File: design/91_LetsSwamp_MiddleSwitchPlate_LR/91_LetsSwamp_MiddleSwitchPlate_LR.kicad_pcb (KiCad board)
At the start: 2 copper layers, 122.6 x 93.3 mm, 0 parts

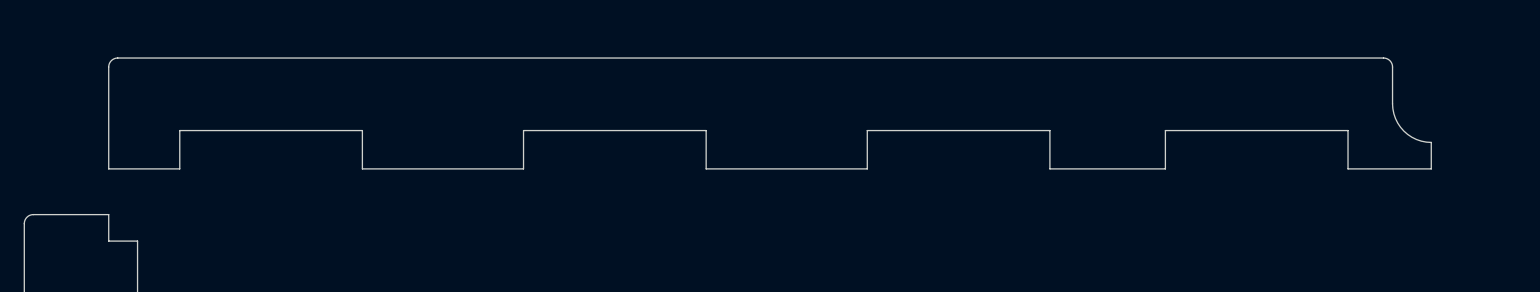
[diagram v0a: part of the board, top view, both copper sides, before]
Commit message: Modify middle plates
avoid to pin sockets and some diodes
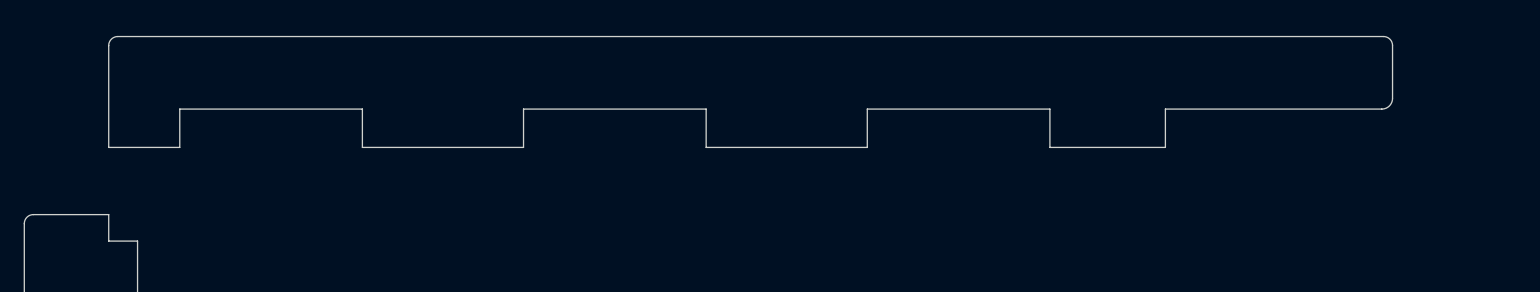
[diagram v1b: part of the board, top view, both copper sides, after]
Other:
- board size 122.6 x 93.3 mm -> 122.6 x 94.5 mm
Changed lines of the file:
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@@
   (general
     (thickness 1.6)
-    (drawings 59)
+    (drawings 56)
     (tracks 0)
     (zones 0)
@@
     (uvia_drill 0.1)
   )
+  (gr_arc (start 61.552092 -15.31093) (end 61.552092 -14.715618) (angle -90) (layer Edge.Cuts) (width 0.05))
+  (gr_line (start 13.989848 -12.590625) (end 5.060152 -12.590625) (layer Edge.Cuts) (width 0.05))
+  (gr_line (start -8.497324 -18.735168) (end 61.647404 -18.735168) (layer Edge.Cuts) (width 0.05))
+  (gr_arc (start -8.497324 -18.235168) (end -8.497324 -18.735168) (angle -90) (layer Edge.Cuts) (width 0.05))
+  (gr_line (start 62.147404 -15.31093) (end 62.147404 -18.235168) (layer Edge.Cuts) (width 0.05))
+  (gr_line (start -8.997324 -12.590625) (end -8.997324 -18.235168) (layer Edge.Cuts) (width 0.05))
+  (gr_line (start -5.060152 -14.715617) (end 5.060152 -14.715617) (layer Edge.Cuts) (width 0.05))
+  (gr_line (start 5.060152 -14.715617) (end 5.060152 -12.590625) (layer Edge.Cuts) (width 0.05))
+  (gr_line (start 49.559772 -12.590625) (end 43.160152 -12.590625) (layer Edge.Cuts) (width 0.05))
+  (gr_line (start 24.110152 -14.715617) (end 24.110152 -12.590625) (layer Edge.Cuts) (width 0.05))
+  (gr_line (start 43.160152 -14.715617) (end 43.160152 -12.590625) (layer Edge.Cuts) (width 0.05))
+  (gr_line (start 49.559772 -14.715617) (end 61.552092 -14.715617) (layer Edge.Cuts) (width 0.05))
+  (gr_line (start 33.039848 -12.590625) (end 24.110152 -12.590625) (layer Edge.Cuts) (width 0.05))
+  (gr_line (start 13.989848 -12.590625) (end 13.989848 -14.715617) (layer Edge.Cuts) (width 0.05))
+  (gr_line (start 13.989848 -14.715617) (end 24.110152 -14.715617) (layer Edge.Cuts) (width 0.05))
+  (gr_line (start -5.060152 -12.590625) (end -8.997324 -12.590625) (layer Edge.Cuts) (width 0.05))
+  (gr_line (start 33.039848 -14.715617) (end 43.160152 -14.715617) (layer Edge.Cuts) (width 0.05))
+  (gr_arc (start 61.647404 -18.235168) (end 62.147404 -18.235168) (angle -90) (layer Edge.Cuts) (width 0.05))
+  (gr_line (start 49.559772 -12.590625) (end 49.559772 -14.715617) (layer Edge.Cuts) (width 0.05))
+  (gr_line (start -5.060152 -12.590625) (end -5.060152 -14.715617) (layer Edge.Cuts) (width 0.05))
+  (gr_line (start 33.039848 -12.590625) (end 33.039848 -14.715617) (layer Edge.Cuts) (width 0.05))
   (gr_line (start 102.65 64.55) (end 104.251328 64.55) (layer Edge.Cuts) (width 0.05))
   (gr_line (start 104.251328 64.55) (end 104.251328 67.05866) (layer Edge.Cuts) (width 0.05))
@@
   (gr_line (start -8.997324 -8.866859) (end -8.997324 -7.4) (layer Edge.Cuts) (width 0.05))
   (gr_line (start 102.65 -6.8) (end 108.929008 -6.8) (layer Edge.Cuts) (width 0.05))
-  (gr_line (start 13.989848 -11.4) (end 5.060152 -11.4) (layer Edge.Cuts) (width 0.05))
-  (gr_line (start 64.293836 -11.4) (end 59.680076 -11.4) (layer Edge.Cuts) (width 0.05))
-  (gr_line (start 49.559772 -11.4) (end 43.160152 -11.4) (layer Edge.Cuts) (width 0.05))
-  (gr_line (start 33.039848 -11.4) (end 24.110152 -11.4) (layer Edge.Cuts) (width 0.05))
-  (gr_line (start 64.293836 -12.866859) (end 64.293836 -11.4) (layer Edge.Cuts) (width 0.05))
-  (gr_line (start 49.559772 -13.524992) (end 59.680076 -13.524992) (layer Edge.Cuts) (width 0.05))
-  (gr_line (start 49.559772 -11.4) (end 49.559772 -13.524992) (layer Edge.Cuts) (width 0.05))
-  (gr_line (start 59.680076 -13.524992) (end 59.680076 -11.4) (layer Edge.Cuts) (width 0.05))
-  (gr_line (start 43.160152 -13.524992) (end 43.160152 -11.4) (layer Edge.Cuts) (width 0.05))
-  (gr_line (start 33.039848 -11.4) (end 33.039848 -13.524992) (layer Edge.Cuts) (width 0.05))
-  (gr_line (start 33.039848 -13.524992) (end 43.160152 -13.524992) (layer Edge.Cuts) (width 0.05))
-  (gr_line (start 24.110152 -13.524992) (end 24.110152 -11.4) (layer Edge.Cuts) (width 0.05))
-  (gr_line (start 13.989848 -13.524992) (end 24.110152 -13.524992) (layer Edge.Cuts) (width 0.05))
-  (gr_line (start 13.989848 -11.4) (end 13.989848 -13.524992) (layer Edge.Cuts) (width 0.05))
-  (gr_line (start 5.060152 -13.524992) (end 5.060152 -11.4) (layer Edge.Cuts) (width 0.05))
-  (gr_line (start -5.060152 -13.524992) (end 5.060152 -13.524992) (layer Edge.Cuts) (width 0.05))
-  (gr_line (start -5.060152 -11.4) (end -5.060152 -13.524992) (layer Edge.Cuts) (width 0.05))
   (gr_line (start 102.65 64.55) (end 102.65 -6.8) (layer Edge.Cuts) (width 0.05))
   (gr_line (start -8.997324 68.55) (end 104.251328 68.55) (layer Edge.Cuts) (width 0.05))
   (gr_line (start -7.4 -7.4) (end -7.4 64.55) (layer Edge.Cuts) (width 0.05))
-  (gr_line (start -5.060152 -11.4) (end -8.997324 -11.4) (layer Edge.Cuts) (width 0.05))
-  (gr_arc (start 61.647404 -17.044543) (end 62.147404 -17.044543) (angle -90) (layer Edge.Cuts) (width 0.05))
   (gr_arc (start 108.429008 6.878578) (end 108.429008 7.378578) (angle -90) (layer Edge.Cuts) (width 0.05))
   (gr_arc (start 108.429008 12.171442) (end 108.929008 12.171442) (angle -90) (layer Edge.Cuts) (width 0.05))
@@
   (gr_arc (start -13.175008 6.878576) (end -13.675008 6.878576) (angle -90) (layer Edge.Cuts) (width 0.05))
   (gr_arc (start -13.175008 -8.366859) (end -13.175008 -8.866859) (angle -90) (layer Edge.Cuts) (width 0.05))
-  (gr_arc (start -8.497324 -17.044543) (end -8.497324 -17.544543) (angle -90) (layer Edge.Cuts) (width 0.05))
   (gr_line (start -13.675008 6.878576) (end -13.675008 -8.366859) (layer Edge.Cuts) (width 0.05))
   (gr_line (start 108.929008 12.171442) (end 108.929008 66.55866) (layer Edge.Cuts) (width 0.05))
-  (gr_line (start -8.497324 -17.544543) (end 61.647404 -17.544543) (layer Edge.Cuts) (width 0.05))
   (gr_line (start 106.397756 7.378578) (end 108.429008 7.378578) (layer Edge.Cuts) (width 0.05))
   (gr_line (start 106.397756 11.671442) (end 108.429008 11.671442) (layer Edge.Cuts) (width 0.05))
@@
   (gr_line (start -11.143756 7.378576) (end -13.175008 7.378576) (layer Edge.Cuts) (width 0.05))
   (gr_line (start -8.997324 -8.866859) (end -13.175008 -8.866859) (layer Edge.Cuts) (width 0.05))
-  (gr_line (start -8.997324 -11.4) (end -8.997324 -17.044543) (layer Edge.Cuts) (width 0.05))
-  (gr_line (start 62.147404 -15.013291) (end 62.147404 -17.044543) (layer Edge.Cuts) (width 0.05))
   (gr_arc (start -11.143756 9.525008) (end -11.143756 11.67144) (angle -180) (layer Edge.Cuts) (width 0.05))
   (gr_arc (start 106.397756 9.52501) (end 106.397756 7.378578) (angle -180) (layer Edge.Cuts) (width 0.05))
-  (gr_arc (start 64.293836 -15.013291) (end 62.147404 -15.013291) (angle -90) (layer Edge.Cuts) (width 0.05))
   (gr_line (start -13.675008 12.17144) (end -13.675008 66.558656) (layer Edge.Cuts) (width 0.05))
   (gr_line (start 108.929008 6.878578) (end 108.929008 -6.8) (layer Edge.Cuts) (width 0.05))
